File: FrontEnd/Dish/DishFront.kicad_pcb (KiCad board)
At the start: 2 copper layers, 83 parts, among them U1 PMA-545G1_Amp

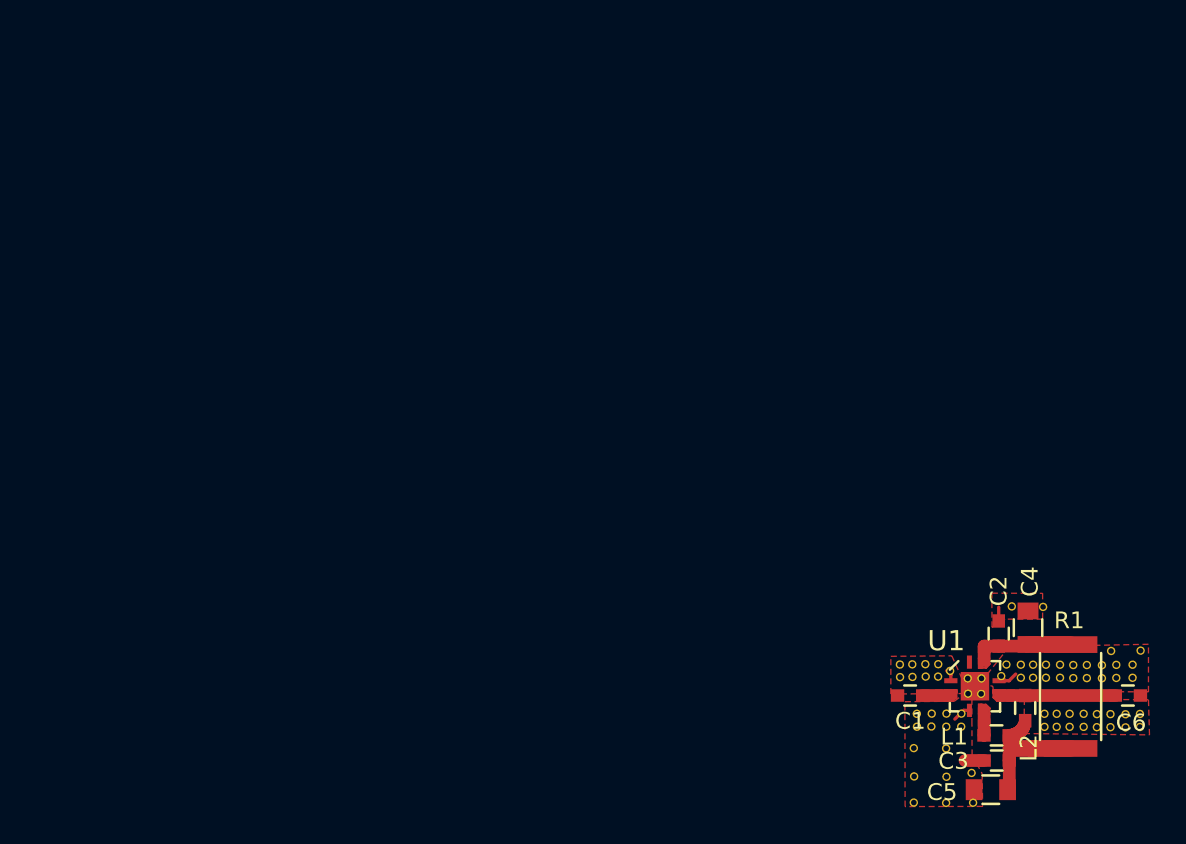
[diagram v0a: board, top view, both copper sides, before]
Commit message: [Removed] clutter text on amplifier block; [Added] basic project for the dish front-end
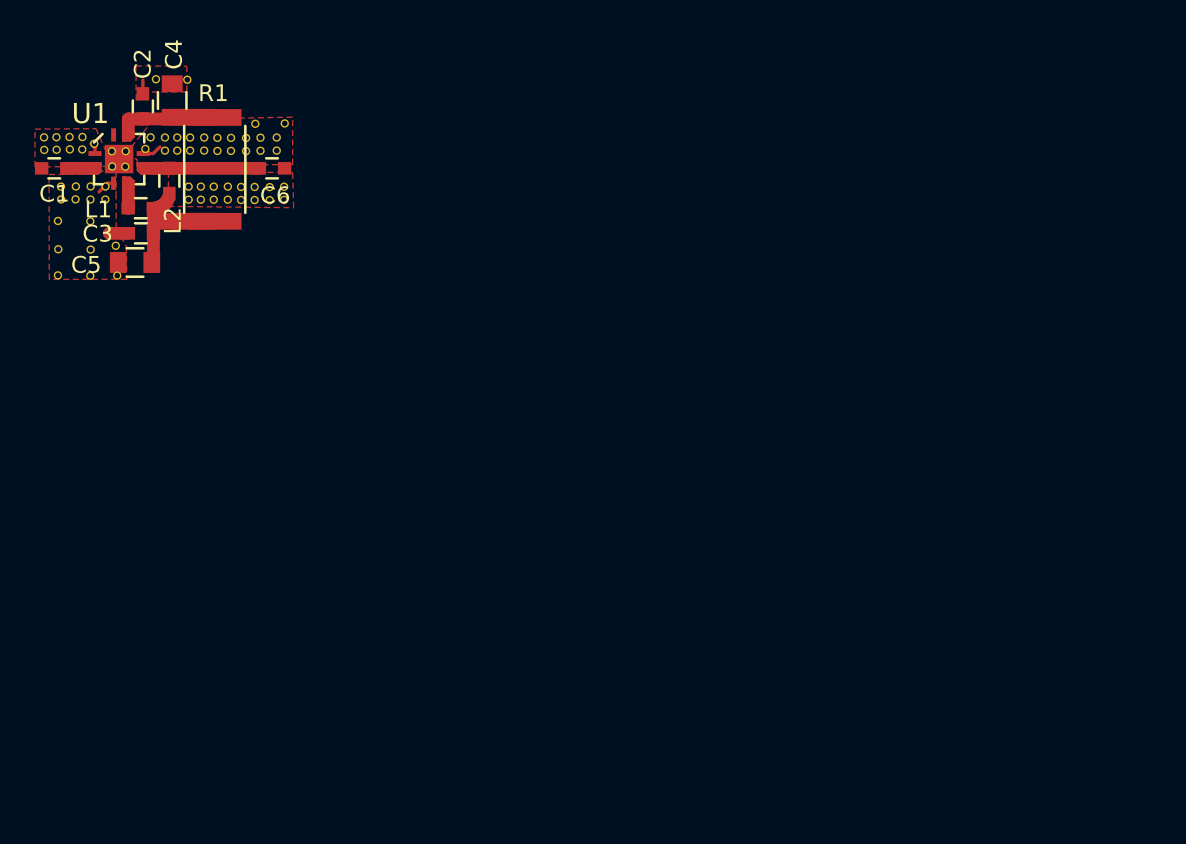
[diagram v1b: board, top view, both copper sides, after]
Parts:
- moved ? 60.0 mm to (98.0, 58.9)
- moved ? 60.0 mm to (88.0, 67.9)
- moved ? 60.0 mm to (85.5, 62.6)
- moved ? 60.0 mm to (89.5, 61.5)
- moved C2 60.0 mm to (89.5, 57.8)
- moved ? 60.0 mm to (88.5, 60.5)
- moved C4 60.0 mm to (91.3, 57.5)
- moved ? 60.0 mm to (86.4, 64.7)
- moved ? 60.0 mm to (95.4, 63.4)
- moved ? 60.0 mm to (94.6, 63.4)
- moved ? 60.0 mm to (95.4, 62.6)
- moved ? 60.0 mm to (94.6, 62.6)
- moved ? 60.0 mm to (97.1, 63.4)
- moved ? 60.0 mm to (96.2, 63.4)
- moved ? 60.0 mm to (97.1, 62.7)
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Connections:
- U1 pad 1: GND -> Net-(U1-Pad1)
- U1 pad 3: GND -> Net-(U1-Pad1)
- U1 pad 6: GND -> Net-(U1-Pad1)
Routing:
- net GND: track 4.90 -> 3.75 mm
- net Net-(U1-Pad1): track 0.00 -> 1.16 mm

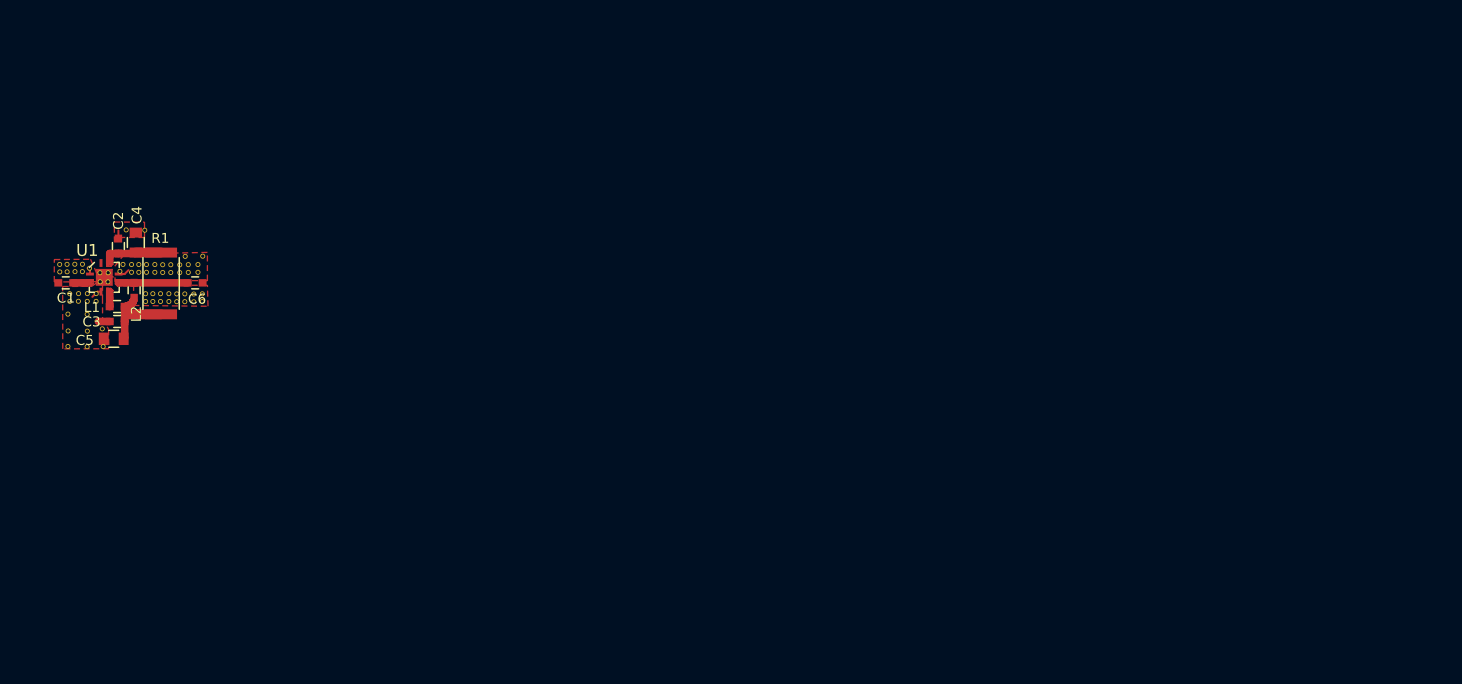
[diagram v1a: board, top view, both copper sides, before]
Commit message: [Added] TI schmitt XOR component; [WIP] Dish front end; [Added] More RF trace adapters
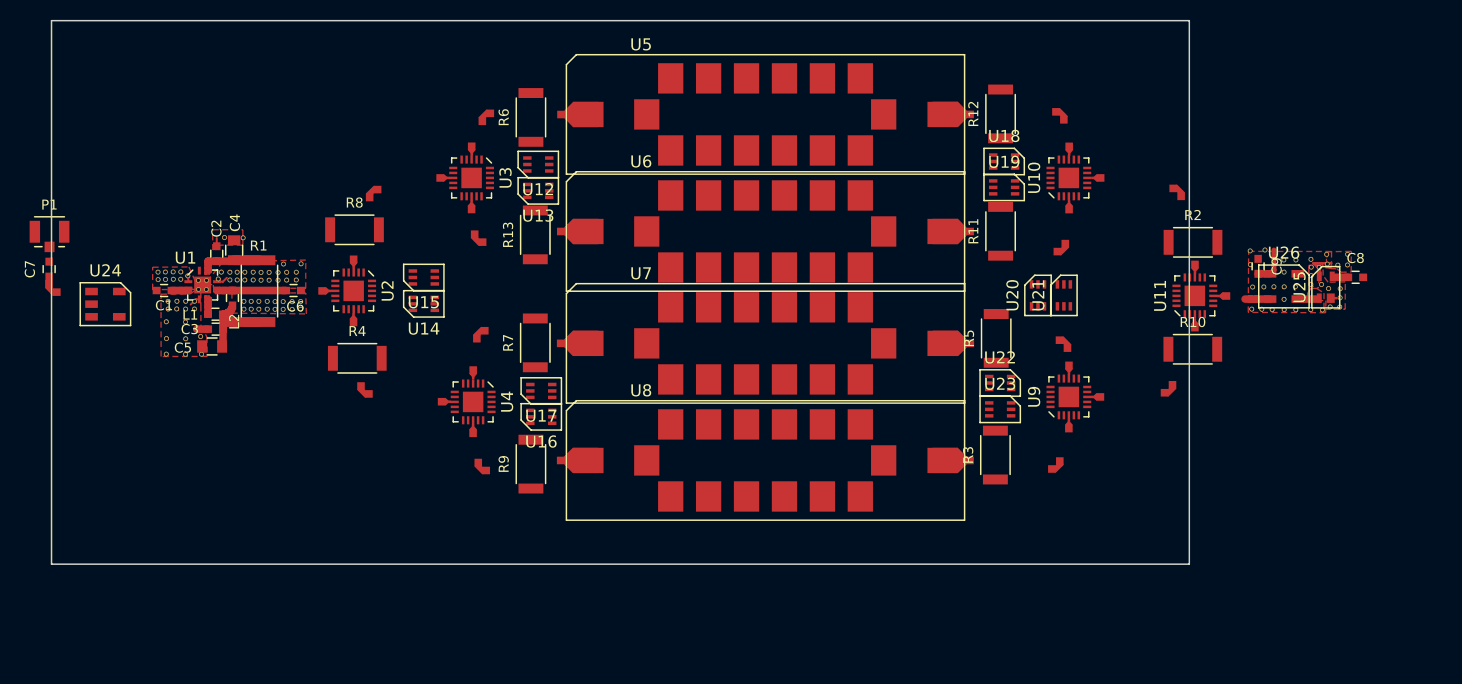
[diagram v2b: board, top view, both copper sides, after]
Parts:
- added ?: , Minicircuits:100mil-30mil, F.Cu at (174.7, 44.6)
- added ?: , Minicircuits:10mil-30mil, F.Cu at (185.0, 53.6)
- added ?: , Minicircuits:10mil-30mil, F.Cu at (197.7, 60.3)
- added ?: , Minicircuits:10mil-30mil, F.Cu at (200.2, 62.9)
- added ?: , Minicircuits:10mil-30mil, F.Cu at (197.7, 65.4)
- added ?: , Minicircuits:10mil-30mil, F.Cu at (185.0, 70.4)
- added ?: , Minicircuits:30mil-30mil_90, F.Cu at (82.6, 62.5)
- added ?: , Minicircuits:10mil-30mil, F.Cu at (110.6, 62.4)
- added ?: , Minicircuits:100mil-30mil, F.Cu at (134.3, 79.4)
- added ?: , Minicircuits:10mil-30mil, F.Cu at (187.6, 73.0)
- added ?: , Minicircuits:10mil-30mil, F.Cu at (185.0, 75.6)
- added ?: , Minicircuits:10mil-30mil, F.Cu at (125.2, 76.0)
- added ?: , Minicircuits:10mil-30mil, F.Cu at (122.6, 73.5)
- added ?: , Minicircuits:10mil-30mil, F.Cu at (125.2, 70.9)
- added ?: , Minicircuits:100mil-30mil, F.Cu at (174.7, 56.4)
- added ?: , Minicircuits:10mil-30mil, F.Cu at (125.0, 53.6)
- added ?: , Minicircuits:10mil-30mil, F.Cu at (122.4, 51.0)
- added ?: , Minicircuits:10mil-30mil, F.Cu at (125.0, 48.4)
- added ?: , Minicircuits:10mil-30mil, F.Cu at (113.2, 59.8)
- added ?: , Minicircuits:10mil-30mil, F.Cu at (113.1, 64.9)
- added ?: , Minicircuits:30mil-30mil_90, F.Cu at (184.1, 80.1)
- added ?: , Minicircuits:30mil-30mil_90, F.Cu at (184.8, 67.3)
- added ?: , Minicircuits:30mil-30mil_90, F.Cu at (195.4, 72.5)
- added ?: , Minicircuits:30mil-30mil_90, F.Cu at (196.2, 52.0)
- added ?: , Minicircuits:30mil-30mil_90, F.Cu at (184.6, 58.3)
- added ?: , Minicircuits:100mil-30mil, F.Cu at (174.7, 67.6)
- added ?: , Minicircuits:30mil-30mil_90, F.Cu at (184.4, 44.4)
- added ?: , Minicircuits:30mil-30mil_90, F.Cu at (125.5, 66.5)
- added ?: , Minicircuits:30mil-30mil_90, F.Cu at (125.4, 57.5)
- added ?: , Minicircuits:30mil-30mil_90, F.Cu at (125.8, 80.4)
- added ?: , Minicircuits:30mil-30mil_90, F.Cu at (126.1, 44.6)
- added ?: , Minicircuits:30mil-30mil_90, F.Cu at (114.8, 52.3)
- added ?: , Minicircuits:30mil-30mil_90, F.Cu at (114.0, 72.7)
- added ?: , DigitalLogic:Via, F.Cu at (210.9, 58.7)
- added ?: , DigitalLogic:Via, F.Cu at (213.0, 58.7)
- added ?: , DigitalLogic:Via, F.Cu at (210.9, 59.6)
- added ?: , Minicircuits:100mil-30mil, F.Cu at (174.7, 79.4)
- added ?: , DigitalLogic:Via, F.Cu at (212.0, 59.8)
- added ?: , DigitalLogic:Via, F.Cu at (213.0, 59.7)
- added ?: , DigitalLogic:Via, F.Cu at (204.7, 58.2)
- added ?: , DigitalLogic:Via, F.Cu at (203.2, 58.3)
- added ?: , DigitalLogic:Via, F.Cu at (203.2, 59.7)
- added ?: , DigitalLogic:Via, F.Cu at (203.4, 64.2)
- added ?: , DigitalLogic:Via, F.Cu at (204.4, 64.2)
- added ?: , DigitalLogic:Via, F.Cu at (205.4, 64.2)
- added ?: , DigitalLogic:Via, F.Cu at (210.5, 64.3)
- added ?: , DigitalLogic:Via, F.Cu at (209.3, 64.2)
- added ?: , Minicircuits:100mil-30mil, F.Cu at (134.4, 44.6)
- added ?: , DigitalLogic:Via, F.Cu at (207.8, 64.2)
- added ?: , DigitalLogic:Via, F.Cu at (206.6, 64.2)
- added ?: , DigitalLogic:Via, F.Cu at (209.3, 59.2)
- added ?: , DigitalLogic:Via, F.Cu at (207.8, 59.2)
- added ?: , DigitalLogic:Via, F.Cu at (206.6, 59.2)
- added ?: , DigitalLogic:Via, F.Cu at (206.6, 60.5)
- added ?: , DigitalLogic:Via, F.Cu at (206.6, 63.2)
- added ?: , DigitalLogic:Via, F.Cu at (203.5, 62.0)
- added ?: , DigitalLogic:Via, F.Cu at (204.6, 62.0)
- added ?: , DigitalLogic:Via, F.Cu at (205.6, 61.9)
- added ?: , Minicircuits:100mil-30mil, F.Cu at (134.4, 56.4)
- added ?: , DigitalLogic:Via, F.Cu at (207.8, 61.9)
- added ?: , DigitalLogic:Via, F.Cu at (206.6, 61.9)
- added ?: , DigitalLogic:Via, F.Cu at (210.1, 60.0)
- added ?: , DigitalLogic:Via, F.Cu at (209.3, 60.0)
- added ?: , DigitalLogic:Via, F.Cu at (209.3, 60.8)
- added ?: , DigitalLogic:Via, F.Cu at (209.3, 61.7)
- added ?: , DigitalLogic:Via, F.Cu at (211.2, 64.0)
- added ?: , DigitalLogic:Via, F.Cu at (212.2, 64.0)
- added ?: , DigitalLogic:Via, F.Cu at (212.2, 63.0)
- added ?: , DigitalLogic:Via, F.Cu at (212.3, 62.1)
- added ?: , Minicircuits:100mil-30mil, F.Cu at (134.3, 67.6)
- added ?: , DigitalLogic:Via, F.Cu at (211.1, 62.1)
- added ?: , DigitalLogic:Via, F.Cu at (210.4, 61.7)
- added ?: , Minicircuits:10mil-30mil, F.Cu at (185.0, 48.4)
- added ?: , Minicircuits:10mil-30mil, F.Cu at (187.6, 51.0)
- added C7: 100pF, Capacitors_SMD:C_0603, F.Cu at (82.6, 60.2)
- added C8: 100pF, Capacitors_SMD:C_0603, F.Cu at (213.8, 61.0)
- added C9: 0.1uF, Capacitors_SMD:C_0603, F.Cu at (204.0, 59.9)
- added P1: BNC, DigitalLogic:UMCC_PCB, F.Cu at (82.6, 56.4)
- added R10: 0R, Resistors_SMD:R_2010, F.Cu at (197.4, 68.2)
- added R11: 0R, Resistors_SMD:R_2010, F.Cu at (178.1, 56.4)
- added R12: 0R, Resistors_SMD:R_2010, F.Cu at (178.1, 44.6)
- added R13: 0R, Resistors_SMD:R_2010, F.Cu at (131.4, 56.7)
- added R2: 0R, Resistors_SMD:R_2010, F.Cu at (197.5, 57.5)
- added R3: 0R, Resistors_SMD:R_2010, F.Cu at (177.6, 78.8)
- added R4: 0R, Resistors_SMD:R_2010, F.Cu at (113.5, 69.1)
- added R5: 0R, Resistors_SMD:R_2010, F.Cu at (177.7, 67.1)
- added R6: 0R, Resistors_SMD:R_2010, F.Cu at (131.0, 44.9)
- added R7: 0R, Resistors_SMD:R_2010, F.Cu at (131.4, 67.6)
- added R8: 0R, Resistors_SMD:R_2010, F.Cu at (113.2, 56.2)
- added R9: 0R, Resistors_SMD:R_2010, F.Cu at (131.0, 79.8)
- added U10: HSWA2-30DR_switch, Minicircuits:MC_DG983-1, F.Cu at (185.0, 51.0)
- added U11: HSWA2-30DR_switch, Minicircuits:MC_DG983-1, F.Cu at (197.7, 62.8)
- added U12: SN74AUP1T86_Schmitt_XOR, DigitalLogic:TI_DCK, F.Cu at (131.7, 49.6)
- added U13: SN74AUP1T86_Schmitt_XOR, DigitalLogic:TI_DCK, F.Cu at (131.7, 52.3)
- added U14: SN74AUP1T86_Schmitt_XOR, DigitalLogic:TI_DCK, F.Cu at (120.2, 63.6)
- added U15: SN74AUP1T86_Schmitt_XOR, DigitalLogic:TI_DCK, F.Cu at (120.2, 61.0)
- added U16: SN74AUP1T86_Schmitt_XOR, DigitalLogic:TI_DCK, F.Cu at (132.0, 75.0)
- added U17: SN74AUP1T86_Schmitt_XOR, DigitalLogic:TI_DCK, F.Cu at (132.0, 72.4)
- added U18: SN74AUP1T86_Schmitt_XOR, DigitalLogic:TI_DCK, F.Cu at (178.5, 49.4)
- added U19: SN74AUP1T86_Schmitt_XOR, DigitalLogic:TI_DCK, F.Cu at (178.5, 52.0)
- added U2: HSWA2-30DR_switch, Minicircuits:MC_DG983-1, F.Cu at (113.2, 62.3)
- added U20: SN74AUP1T86_Schmitt_XOR, DigitalLogic:TI_DCK, F.Cu at (181.9, 62.8)
- added U21: SN74AUP1T86_Schmitt_XOR, DigitalLogic:TI_DCK, F.Cu at (184.5, 62.8)
- added U22: SN74AUP1T86_Schmitt_XOR, DigitalLogic:TI_DCK, F.Cu at (178.1, 71.6)
- added U23: SN74AUP1T86_Schmitt_XOR, DigitalLogic:TI_DCK, F.Cu at (178.1, 74.2)
- added U24: MC_DBTC-17-5_Coupler, Minicircuits:MC_AT790-1, F.Cu at (88.2, 63.7)
- added U25: PSA4-5043_Amp, Minicircuits:MC_MMM1362, F.Cu at (210.8, 62.0)
- added U26: MC_TCBT-2R5G_BiasT, Minicircuits:MC_GU1604, F.Cu at (206.6, 61.9)
- added U3: HSWA2-30DR_switch, Minicircuits:MC_DG983-1, F.Cu at (125.0, 51.0)
- added U4: HSWA2-30DR_switch, Minicircuits:MC_DG983-1, F.Cu at (125.2, 73.5)
- added U5: MC_HQ1157_Bandpass, Minicircuits:MC_HQ1157, F.Cu at (154.5, 44.6)
- added U6: MC_HQ1157_Bandpass, Minicircuits:MC_HQ1157, F.Cu at (154.5, 56.4)
- added U7: MC_HQ1157_Bandpass, Minicircuits:MC_HQ1157, F.Cu at (154.5, 67.6)
- added U8: MC_HQ1157_Bandpass, Minicircuits:MC_HQ1157, F.Cu at (154.5, 79.4)
- added U9: HSWA2-30DR_switch, Minicircuits:MC_DG983-1, F.Cu at (185.0, 73.0)
- moved C5 9.91 mm to (98.9, 67.9)
- moved ? 9.91 mm to (101.5, 60.5)
- moved ? 9.91 mm to (101.5, 61.2)
- moved ? 9.91 mm to (93.5, 61.2)
- moved ? 9.91 mm to (95.4, 63.4)
- moved ? 9.91 mm to (94.5, 63.4)
- moved ? 9.91 mm to (95.8, 60.4)
- moved ? 9.91 mm to (95.0, 61.2)
- moved ? 9.91 mm to (98.4, 61.3)
- moved ? 9.91 mm to (99.4, 62.3)
- moved ? 9.91 mm to (100.2, 57.0)
- moved ? 9.91 mm to (97.9, 68.7)
- moved ? 9.91 mm to (96.3, 68.7)
- moved ? 9.91 mm to (96.3, 65.5)
- moved ? 9.91 mm to (105.3, 64.2)
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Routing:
- net GND: track 3.75 -> 7.68 mm
- net +5V: track 8.57 -> 12.3 mm
- net Net-(U26-Pad2): track 0.00 -> 2.64 mm
- net Net-(U25-Pad1): track 0.00 -> 1.90 mm
- net Net-(C8-Pad1): track 0.00 -> 1.35 mm
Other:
- board outline added: 114.3 x 54.6 mm

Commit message: [Fixed] 30mil RF Miter to maintain constant impedance; [Added] 30 mil 90-degree arc; [WIP] Dish front end
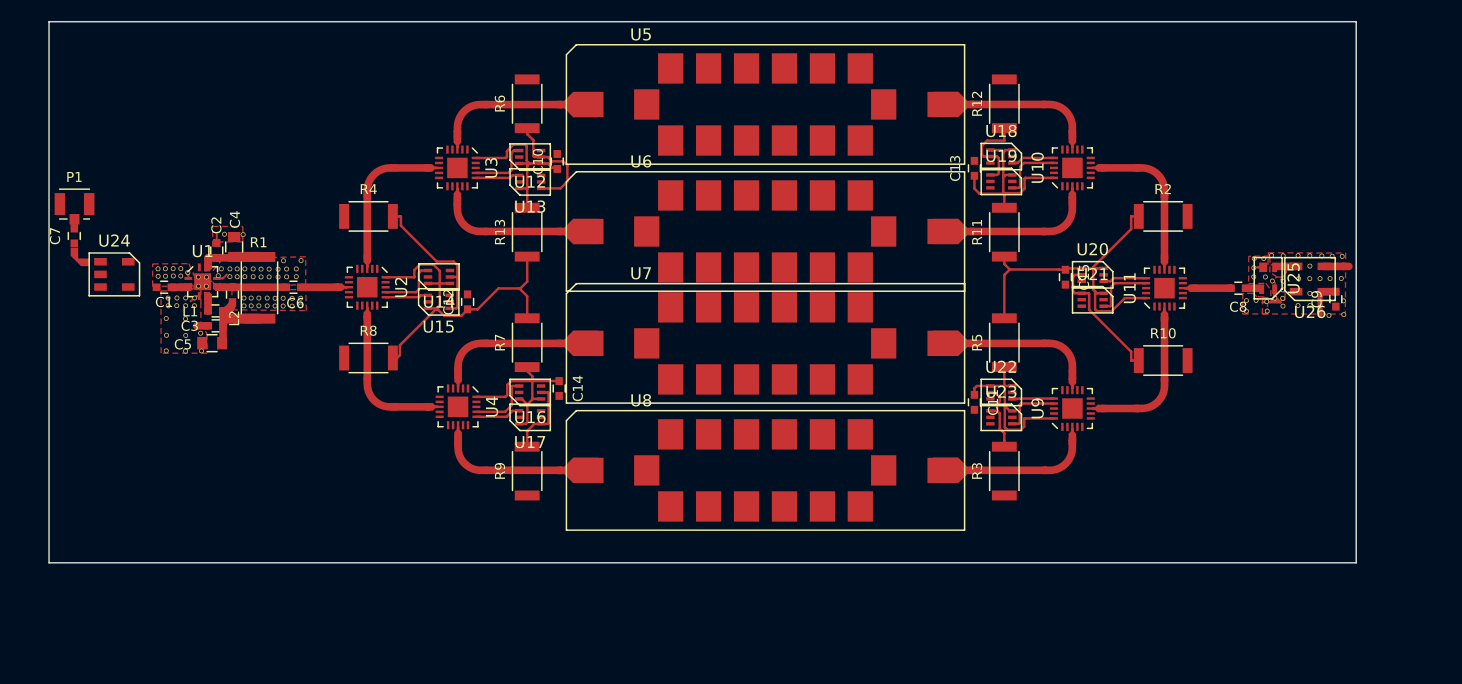
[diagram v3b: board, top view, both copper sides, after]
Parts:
- removed the ? at (184.1, 80.1)
- removed the ? at (184.8, 67.3)
- removed the ? at (195.4, 72.5)
- removed the ? at (196.2, 52.0)
- removed the ? at (184.6, 58.3)
- removed the ? at (184.4, 44.4)
- removed the ? at (125.5, 66.5)
- removed the ? at (125.4, 57.5)
- removed the ? at (125.8, 80.4)
- removed the ? at (126.1, 44.6)
- removed the ? at (114.8, 52.3)
- removed the ? at (114.0, 72.7)
- added ?: , Minicircuits:30mil-30mil_90_Arc, F.Cu at (116.8, 52.3)
- added ?: , Minicircuits:30mil-30mil_90_Arc, F.Cu at (183.1, 78.1)
- added ?: , Minicircuits:30mil-30mil_90_Arc, F.Cu at (183.1, 69.9)
- added ?: , Minicircuits:30mil-30mil_90_Arc, F.Cu at (192.3, 52.3)
- added ?: , Minicircuits:30mil-30mil_90_Arc, F.Cu at (125.9, 54.1)
- added ?: , Minicircuits:30mil-30mil_90_Arc, F.Cu at (125.9, 45.9)
- added ?: , Minicircuits:30mil-30mil_90_Arc, F.Cu at (116.8, 71.7)
- added ?: , Minicircuits:30mil-30mil_90_Arc, F.Cu at (125.9, 78.1)
- added ?: , Minicircuits:30mil-30mil_90_Arc, F.Cu at (125.9, 69.9)
- added ?: , Minicircuits:30mil-30mil_90_Arc, F.Cu at (183.1, 45.9)
- added ?: , Minicircuits:30mil-30mil_90_Arc, F.Cu at (183.1, 54.1)
- added ?: , Minicircuits:30mil-30mil_90_Arc, F.Cu at (192.3, 71.9)
- added C10: 0.1uF, Capacitors_SMD:C_0603, F.Cu at (133.6, 49.3)
- added C11: 0.1uF, Capacitors_SMD:C_0603, F.Cu at (175.5, 73.5)
- added C12: 0.1uF, Capacitors_SMD:C_0603, F.Cu at (124.6, 63.5)
- added C13: 0.1uF, Capacitors_SMD:C_0603, F.Cu at (175.5, 50.0)
- added C14: 0.1uF, Capacitors_SMD:C_0603, F.Cu at (133.8, 72.2)
- added C15: 0.1uF, Capacitors_SMD:C_0603, F.Cu at (184.7, 61.0)
- moved R4 14.3 mm to (114.6, 54.9)
- moved R8 13.0 mm to (114.6, 69.1)
- moved C8 11.8 mm to (202.0, 62.1), turned to 180 degrees
- moved ? 11.7 mm to (202.8, 64.4), turned to 180 degrees
- moved ? 11.4 mm to (212.6, 64.7), turned to 180 degrees
- moved ? 10.8 mm to (202.8, 63.3), turned to 180 degrees
- moved ? 10.5 mm to (212.5, 58.9), turned to 180 degrees
- moved ? 10.0 mm to (212.6, 63.3), turned to 180 degrees
- moved ? 9.88 mm to (203.6, 59.1), turned to 180 degrees
- moved ? 9.20 mm to (211.1, 64.8), turned to 180 degrees
- moved ? 9.18 mm to (203.6, 60.0), turned to 180 degrees
- moved ? 8.95 mm to (212.4, 61.1), turned to 180 degrees
- moved ? 8.94 mm to (203.8, 63.3), turned to 180 degrees
- moved ? 8.85 mm to (211.4, 58.9), turned to 180 degrees
- moved ? 8.77 mm to (203.6, 60.9), turned to 180 degrees
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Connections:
- ? pad 1: (no net) -> Net-(U10-Pad13) (x2)
- ? pad 2: (no net) -> Net-(U10-Pad13)
- ? pad 1: (no net) -> Net-(U10-Pad3) (x2)
- ? pad 2: (no net) -> Net-(U10-Pad3) (x2)
- ? pad 1: (no net) -> Net-(U7-Pad8) (x2)
- ? pad 2: (no net) -> Net-(U7-Pad8) (x2)
- ? pad 1: (no net) -> AMP1_Out
- ? pad 2: (no net) -> AMP1_Out
- ? pad 1: (no net) -> Net-(U4-Pad13) (x2)
- ? pad 2: (no net) -> Net-(U4-Pad13) (x2)
- ? pad 1: (no net) -> Net-(U8-Pad8) (x2)
- ? pad 2: (no net) -> Net-(U8-Pad8) (x2)
- ? pad 1: (no net) -> Net-(U3-Pad3) (x2)
- ? pad 2: (no net) -> Net-(U3-Pad3) (x2)
- ? pad 1: (no net) -> Net-(U3-Pad13) (x2)
- ? pad 2: (no net) -> Net-(U3-Pad13) (x2)
- ? pad 1: (no net) -> Net-(U4-Pad3) (x2)
- ? pad 2: (no net) -> Net-(U4-Pad3) (x2)
- ? pad 1: (no net) -> Net-(U10-Pad8) (x2)
- ? pad 2: (no net) -> Net-(U10-Pad8) (x2)
- ? pad 1: (no net) -> AMP2_In
- ? pad 2: (no net) -> AMP2_In
- ? pad 1: (no net) -> Net-(U11-Pad3) (x2)
- ? pad 2: (no net) -> Net-(U11-Pad3) (x2)
- ? pad 1: (no net) -> Net-(U2-Pad13) (x2)
- ? pad 2: (no net) -> Net-(U2-Pad13) (x2)
- ? pad 1: (no net) -> Net-(U2-Pad3) (x2)
- ? pad 2: (no net) -> Net-(U2-Pad3) (x2)
- C6 pad 1: Net-(C6-Pad1) -> AMP1_Out
- C8 pad 2: Net-(C8-Pad2) -> AMP2_In
- U10 pad 18: Net-(U10-Pad18) -> GND
- U10 pad 19: Net-(U10-Pad19) -> GND
- U10 pad 20: Net-(U10-Pad20) -> +3V3
- U11 pad 18: Net-(U11-Pad18) -> GND
- U11 pad 19: Net-(U11-Pad19) -> GND
- U11 pad 20: Net-(U11-Pad20) -> +3V3
- U11 pad 8: Net-(U11-Pad8) -> AMP2_In
- U2 pad 18: Net-(U2-Pad18) -> GND
- U2 pad 19: Net-(U2-Pad19) -> GND
- U2 pad 20: Net-(U2-Pad20) -> +3V3
- U2 pad 8: Net-(U2-Pad8) -> AMP1_Out
- U3 pad 18: Net-(U3-Pad18) -> GND
- U3 pad 19: Net-(U3-Pad19) -> GND
- U3 pad 20: Net-(U3-Pad20) -> +3V3
- U4 pad 18: Net-(U4-Pad18) -> GND
- U4 pad 19: Net-(U4-Pad19) -> GND
- U4 pad 20: Net-(U4-Pad20) -> +3V3
- U9 pad 18: Net-(U9-Pad18) -> GND
- U9 pad 19: Net-(U9-Pad19) -> GND
- U9 pad 20: Net-(U9-Pad20) -> +3V3
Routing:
- net +3V3: track 0.00 -> 144.0 mm
- net S2CTRL: track 0.00 -> 35.3 mm
- net S1_CTRL: track 0.00 -> 28.2 mm
- net Net-(U11-Pad3): track 0.00 -> 10.1 mm
- net Net-(U10-Pad8): track 0.00 -> 10.1 mm
- net Net-(U2-Pad13): track 0.00 -> 9.93 mm
- net Net-(U2-Pad3): track 0.00 -> 9.85 mm
- net Net-(U3-Pad13): track 0.00 -> 8.52 mm
- net Net-(U7-Pad8): track 0.00 -> 8.51 mm
- net Net-(U3-Pad3): track 0.00 -> 8.49 mm
- net Net-(U4-Pad13): track 0.00 -> 8.45 mm
- net Net-(U4-Pad3): track 0.00 -> 8.44 mm
- net Net-(U10-Pad3): track 0.00 -> 8.35 mm
- net Net-(U10-Pad13): track 0.00 -> 8.33 mm
- net Net-(U8-Pad8): track 0.00 -> 8.18 mm
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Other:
- board size 114.3 x 54.6 mm -> 131.3 x 54.4 mm
- board text added: "186mA"
- board text added: "66mA"
